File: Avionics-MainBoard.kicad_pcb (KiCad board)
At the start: 2 copper layers, 90.2 x 95.9 mm, 251 parts, among them J1 USB_C_Receptacle_USB2.0, J10 1824543, J11 1824527, J12 1824527, J13 1824527, J14 200528-0100, J15 200528-0100, J16 200528-0100, J17 1824543, J18 200528-0100, J19 200528-0100, J2 200528-0100, J3 Conn_01x06, J4 200528-0100, J5 Micro_SD_Card_Det2, J7 U.FL-R-SMT-1, J9 200528-0100, Q1 IRLML2803, Q14 MMBT2907, Q15 MMBT2907, Q16 NX3008NBKS, Q2 NX3008NBKS, Q21 MBT2222ADW1T1, Q22 NX3008NBKS, Q23 MBT2222ADW1T1, Q24 NX3008NBKS, Q25 MBT2222ADW1T1, Q26 NX3008NBKS, Q27 MBT2222ADW1T1, Q28 NX3008NBKS, Q29 MBT2222ADW1T1, Q3 MBT2222ADW1T1, Q30 MBT2222ADW1T1, Q4 NX3008NBKS, Q43 MBT2222ADW1T1, Q44 NX3008NBKS, Q45 MBT2222ADW1T1, Q46 NX3008NBKS, Q47 MBT2222ADW1T1, Q48 NX3008NBKS, Q49 MBT2222ADW1T1, Q5 MBT2222ADW1T1, Q50 NX3008NBKS, Q51 MBT2222ADW1T1, Q52 NX3008NBKS, Q53 MBT2222ADW1T1, SW1 SW_Omron_B3FS, SW2 SW_Omron_B3FS, U1 W25Q64JVSS, U10 BTS5090-1EJA, U14 ADM1176-1ARMZ-R7, U15 TPS7A4501DCQT, U16 ADM1176-1ARMZ-R7, U17 TPS54226PWPR, U18 ADM1176-1ARMZ-R7, U2 RP2040, U3 MAX706RESA+, U4 DS3231M, U5 BNO085, U6 USBLC6-2SC6, U7 E22-900M30S, U8 S1216V8, U9 BQ25883RGER, Y1 12MHz, Y2 32.768kHz

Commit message: temp
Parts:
- removed Q21, Q23, Q25, Q27, Q43, Q45, Q47, Q49, Q51, Q53: MBT2222ADW1T1, Package_TO_SOT_SMD:SOT-363_SC-70-6
- removed R99: DNI (0R), Resistor_SMD:R_0603_1608Metric
- added ?: , , F.Cu at (113.8, 57.1)
- added ?: , , F.Cu at (190.0, 142.9)
- added ?: , , F.Cu at (187.5, 57.1)
- added ?: , , F.Cu at (110.0, 142.9)
- added Q10: MBT2222ADW1T1, Package_TO_SOT_SMD:SOT-363_SC-70-6, F.Cu at (-51.2, -65.3)
- added Q11: MBT2222ADW1T1, Package_TO_SOT_SMD:SOT-363_SC-70-6, F.Cu at (-30.7, -69.3)
- added Q12: MBT2222ADW1T1, Package_TO_SOT_SMD:SOT-363_SC-70-6, F.Cu at (37.8, -60.9)
- added Q13: MBT2222ADW1T1, Package_TO_SOT_SMD:SOT-363_SC-70-6, F.Cu at (37.8, -41.3)
- added Q17: MBT2222ADW1T1, Package_TO_SOT_SMD:SOT-363_SC-70-6, F.Cu at (-51.2, -30.1)
- added Q6: MBT2222ADW1T1, Package_TO_SOT_SMD:SOT-363_SC-70-6, F.Cu at (48.1, -60.9)
- added Q7: MBT2222ADW1T1, Package_TO_SOT_SMD:SOT-363_SC-70-6, F.Cu at (-40.9, -69.3)
- added Q8: MBT2222ADW1T1, Package_TO_SOT_SMD:SOT-363_SC-70-6, F.Cu at (48.1, -41.3)
- added Q9: MBT2222ADW1T1, Package_TO_SOT_SMD:SOT-363_SC-70-6, F.Cu at (-40.9, -30.1)
- added Q99: NX3008NBKS, Package_TO_SOT_SMD:SOT-363_SC-70-6, F.Cu at (-40.9, -26.2)
- added R22: 200K, Resistor_SMD:R_0603_1608Metric, F.Cu at (-45.1, -15.8)
- BT1, C60, C61, C62, J12, J13, R116, U4, U7: moved to F.Cu
- Q14, R49, R50, R51, R52: moved to B.Cu
- Q2: value NX3008NBKS -> MBT2222ADW1T1
- R15: value 10K -> DNI (0R)
- R17: value 200K -> 10K
- moved J19 267.0 mm to (170.0, 143.1), turned to 0 degrees
- moved C20 260.1 mm to (-34.8, -45.4), turned to 0 degrees
- moved R8 259.1 mm to (-34.8, -37.9), turned to 0 degrees
- moved R9 258.5 mm to (-34.8, -35.4), turned to 0 degrees
- moved U5 256.4 mm to (-29.2, -48.8)
- moved C21 255.7 mm to (-34.8, -42.9), turned to 0 degrees
- moved Y2 250.4 mm to (-30.3, -44.3)
- moved C22 249.3 mm to (-34.8, -40.4), turned to 0 degrees
- moved C61 245.8 mm to (11.0, -59.1), turned to 0 degrees
- moved C18 244.3 mm to (-34.8, -50.5)
- moved C19 244.3 mm to (-34.8, -47.9)
- moved C60 242.3 mm to (11.0, -61.6), turned to 0 degrees
- moved R122 240.0 mm to (25.4, -60.5), turned to 0 degrees
- moved C63 236.4 mm to (11.0, -54.1), turned to 0 degrees
- moved J18 235.9 mm to (130.0, 143.1), turned to 0 degrees
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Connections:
- C23 pad 1: (no net) -> Net-(Q99B-G1)
- J15 pad 6: GND -> /MCU_IO/Jetson_CSn
- J15 pad 7: /MCU_IO/MCU_TX_Jetson -> /MCU_IO/SPI1_MOSI
- J15 pad 8: GND -> /MCU_IO/SPI1_CLK
- J15 pad 9: /MCU_IO/MCU_RX_Jetson -> /MCU_IO/SPI1_MISO
- J18 pad 10: /MCU_IO/I2C0_SCL -> /MCU_IO/I2C0_SDA
- J18 pad 9: /MCU_IO/I2C0_SDA -> /MCU_IO/I2C0_SCL
- J19 pad 5: /MCU_IO/I2C0_SCL -> /MCU_IO/I2C0_SDA
- J19 pad 6: /MCU_IO/I2C0_SDA -> /MCU_IO/I2C0_SCL
- J2 pad 10: /MCU_IO/I2C0_SCL -> /MCU_IO/I2C0_SDA
- J2 pad 9: /MCU_IO/I2C0_SDA -> /MCU_IO/I2C0_SCL
- J4 pad 10: /MCU_IO/I2C0_SCL -> /MCU_IO/I2C0_SDA
- J4 pad 9: /MCU_IO/I2C0_SDA -> /MCU_IO/I2C0_SCL
- Q14 pad 3: /MCU_IO/SD_MISO -> /LoRa Power/MISO
- Q2 pad 1: GND -> /MCU_IO/I2C1_SDA
- Q2 pad 2: (no net) -> Net-(Q2A-B1)
- Q2 pad 3: (no net) -> /MCU_IO/I2C1_SDA
- Q2 pad 4: GND -> /USB/CHG_SDA
- Q2 pad 5: (no net) -> Net-(Q28A-D1)
- Q2 pad 6: (no net) -> /USB/CHG_SDA
- Q3 pad 2: (no net) -> Net-(Q3A-B1)
- Q3 pad 4: /IMU/IMU_SCL -> /IMU/IMU_SDA
- Q3 pad 5: (no net) -> Net-(Q3B-B2)
- Q3 pad 6: /IMU/IMU_SCL -> /IMU/IMU_SDA
- Q4 pad 6: Net-(Q4A-D1) -> Net-(Q10B-B2)
- Q44 pad 6: Net-(Q44A-D1) -> Net-(Q3B-B2)
- Q5 pad 1: /MCU_IO/I2C1_SCL -> /MCU_IO/I2C0_SCL
- Q5 pad 3: /MCU_IO/I2C1_SCL -> /MCU_IO/I2C0_SCL
- Q5 pad 4: /LoRa Power/I2C Protection3/SCL_DEVICE -> /RTC/RTC_SCL
- Q5 pad 5: Net-(Q4A-D1) -> Net-(Q46A-D1)
- Q5 pad 6: /LoRa Power/I2C Protection3/SCL_DEVICE -> /RTC/RTC_SCL
- R104 pad 2: /MCU_IO/I2C0_SCL -> /MCU_IO/I2C0_SDA
- R105 pad 1: Net-(Q43A-B1) -> Net-(Q2A-B1)
- R13 pad 1: (no net) -> Net-(Q9A-B1)
- R13 pad 2: (no net) -> Net-(Q99A-D1)
- R14 pad 2: (no net) -> Net-(Q99A-G2)
- R15 pad 1: +3V3 -> /IMU/IMU_SCL
- R15 pad 2: (no net) -> /MCU_IO/I2C0_SDA
- R16 pad 2: /IMU/IMU_SCL -> Net-(Q99A-D1)
- R163 pad 1: Net-(Q45A-B1) -> Net-(Q3A-B1)
- R163 pad 2: Net-(Q44A-D1) -> Net-(Q3B-B2)
- R165 pad 2: /MCU_IO/I2C0_SDA -> /MCU_IO/I2C0_SCL
- R166 pad 2: Net-(Q44A-D1) -> Net-(Q3B-B2)
- R169 pad 1: Net-(Q47A-B1) -> Net-(Q5A-B1)
- R17 pad 1: /IMU/IMU_SCL -> +3V3
- R17 pad 2: (no net) -> /IMU/IMU_SCL
- R171 pad 2: /MCU_IO/I2C0_SDA -> /MCU_IO/I2C0_SCL
- R18 pad 1: Net-(Q5A-B1) -> Net-(Q10A-B1)
- R18 pad 2: Net-(Q4A-D1) -> Net-(Q10B-B2)
- R20 pad 2: Net-(Q4A-D1) -> Net-(Q10B-B2)
- R51 pad 2: /MCU_IO/SD_CLK -> /LoRa Power/CLK
- R52 pad 2: /MCU_IO/SD_MOSI -> /LoRa Power/MOSI
- R57 pad 2: /LoRa Power/CSn -> /LoRa Power/LoRa_CSn
- U2 pad 11: /LoRa Power/MISO -> unconnected-(U2-GPIO8-Pad11)
- U2 pad 12: /LoRa Power/CSn -> unconnected-(U2-GPIO9-Pad12)
- U2 pad 13: /LoRa Power/CLK -> unconnected-(U2-GPIO10-Pad13)
- U2 pad 14: /LoRa Power/MOSI -> unconnected-(U2-GPIO11-Pad14)
- U2 pad 15: /MCU_IO/LoRa_EN -> unconnected-(U2-GPIO12-Pad15)
- U2 pad 16: /LoRa Power/LoRa_RSTn -> unconnected-(U2-GPIO13-Pad16)
- U2 pad 17: /LoRa Power/LoRa_BUSY -> unconnected-(U2-GPIO14-Pad17)
- U2 pad 18: /MCU_IO/WDT_WDI -> unconnected-(U2-GPIO15-Pad18)
- U2 pad 2: /MCU_IO/I2C0_SDA -> unconnected-(U2-GPIO0-Pad2)
- U2 pad 27: /MCU_IO/MCU_TX_Jetson -> /LoRa Power/MISO
- U2 pad 28: /MCU_IO/MCU_RX_Jetson -> /LoRa Power/LoRa_CSn
- U2 pad 29: /IMU/IMU_INTn -> /LoRa Power/CLK
- U2 pad 3: /MCU_IO/I2C0_SCL -> unconnected-(U2-GPIO1-Pad3)
- U2 pad 30: /IMU/IMU_RSTn -> /LoRa Power/MOSI
- U2 pad 31: /MCU_IO/SD_MISO -> /LoRa Power/LoRa_RX_EN
- U2 pad 32: /MCU_IO/SD_CSn -> /LoRa Power/LoRa_RSTn
- U2 pad 34: /MCU_IO/SD_CLK -> /LoRa Power/LoRa_TX_EN
- U2 pad 35: /MCU_IO/SD_MOSI -> /LoRa Power/LoRa_BUSY
- U2 pad 36: /MCU_IO/Jetson_EN -> /LoRa Power/LoRa_DIO2
- U2 pad 37: /MCU_IO/Battery_ALERT -> /LoRa Power/LoRa_DIO1
- U2 pad 38: /LoRa Power/LoRa_DIO1 -> /MCU_IO/SD_CSn
- U2 pad 39: /LoRa Power/LoRa_DIO2 -> unconnected-(U2-GPIO27_ADC1-Pad39)
- U2 pad 4: /MCU_IO/I2C1_SDA -> unconnected-(U2-GPIO2-Pad4)
- U2 pad 40: /LoRa Power/LoRa_RX_EN -> unconnected-(U2-GPIO28_ADC2-Pad40)
- U2 pad 41: /LoRa Power/LoRa_TX_EN -> unconnected-(U2-GPIO29_ADC3-Pad41)
- U2 pad 5: /MCU_IO/I2C1_SCL -> unconnected-(U2-GPIO3-Pad5)
- U2 pad 6: /GPS Power/GPS_RX_MCU -> unconnected-(U2-GPIO4-Pad6)
- U2 pad 7: /GPS Power/GPS_TX_MCU -> unconnected-(U2-GPIO5-Pad7)
- U2 pad 8: /MCU_IO/GPS_EN -> unconnected-(U2-GPIO6-Pad8)
- U2 pad 9: /MCU_IO/3V3_RST -> unconnected-(U2-GPIO7-Pad9)
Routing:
- net /LoRa Power/LoRa_DIO2: track 0.00 -> 60.3 mm
- net /LoRa Power/LoRa_TX_EN: track 0.00 -> 58.3 mm
- net /LoRa Power/LoRa_RX_EN: track 0.00 -> 56.9 mm
- net /LoRa Power/MOSI: track 0.00 -> 43.8 mm, vias 0 -> 1
- net /LoRa Power/CLK: track 0.00 -> 41.8 mm, vias 0 -> 1
- net /LoRa Power/LoRa_DIO1: track 0.00 -> 36.2 mm
- net /LoRa Power/MISO: track 0.00 -> 35.0 mm, vias 0 -> 2
- net /LoRa Power/LoRa_BUSY: track 0.00 -> 33.9 mm
- net /LoRa Power/LoRa_RSTn: track 0.00 -> 31.8 mm
- net /LoRa Power/LoRa_CSn: track 0.00 -> 25.1 mm
- net /MCU_IO/SD_CSn: track 0.00 -> 24.3 mm
- net /Main Power/+3V3_PS: track 20.1 -> 0.00 mm
- net Net-(Q15-B): track 0.00 -> 7.83 mm
- net /LoRa Power/LoRa_MISO: track 0.00 -> 7.75 mm
- net /LoRa Power/LoRa_MOSI: track 0.00 -> 7.69 mm
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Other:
- copper layers 2 -> 4

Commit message: v1 done
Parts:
- removed ? (x4): , 
- removed C10: 2u2, Capacitor_SMD:C_0603_1608Metric
- removed D4, D5: 10V, Diode_SMD:D_SOD-123F
- removed R53, R54: 10K, Resistor_SMD:R_0603_1608Metric
- added C25: 2u2, Capacitor_SMD:C_0603_1608Metric, F.Cu at (149.5, 96.0)
- added D1: NUP2105L, Package_TO_SOT_SMD:SOT-23, F.Cu at (183.0, 128.0)
- added D2: NUP2105L, Package_TO_SOT_SMD:SOT-23, F.Cu at (183.0, 131.6)
- added H1: MountingHole_Pad, MountingHole:MountingHole_3.2mm_M3_DIN965_Pad_TopBottom, F.Cu at (113.8, 57.1)
- added H2: MountingHole_Pad, MountingHole:MountingHole_3.2mm_M3_DIN965_Pad_TopBottom, F.Cu at (187.4, 57.1)
- added H3: MountingHole_Pad, MountingHole:MountingHole_3.2mm_M3_DIN965_Pad_TopBottom, F.Cu at (190.1, 142.8)
- added H4: MountingHole_Pad, MountingHole:MountingHole_3.2mm_M3_DIN965_Pad_TopBottom, F.Cu at (110.0, 142.9)
- added J6: 200528-0100, Argus-Connectors:Molex_200528-0100_1x10-1MP_P1.00mm_Horizontal, F.Cu at (190.1, 130.0)
- added R23: 10K, Resistor_SMD:R_0603_1608Metric, B.Cu at (147.0, 113.0)
- added R24: 10K, Resistor_SMD:R_0603_1608Metric, B.Cu at (147.0, 116.5)
- added R25: 10k, Resistor_SMD:R_0603_1608Metric, F.Cu at (150.5, 113.0)
- added R26: 10k, Resistor_SMD:R_0603_1608Metric, F.Cu at (152.0, 113.0)
- added R27: 680R, Resistor_SMD:R_0603_1608Metric, F.Cu at (157.5, 125.5)
- added R28: 120R, Resistor_SMD:R_0603_1608Metric, F.Cu at (151.5, 125.0)
- added R29: 680R, Resistor_SMD:R_0603_1608Metric, F.Cu at (157.5, 128.5)
- added R30: 680R, Resistor_SMD:R_0603_1608Metric, F.Cu at (162.0, 132.0)
- added R31: 120R, Resistor_SMD:R_0603_1608Metric, F.Cu at (148.5, 125.0)
- added R32: 680R, Resistor_SMD:R_0603_1608Metric, F.Cu at (162.0, 129.0)
- added R33: 2k2, Resistor_SMD:R_0603_1608Metric, F.Cu at (121.3, 67.0)
- added U12: ADM1491EBR, Package_SO:SOIC-14_3.9x8.7mm_P1.27mm, F.Cu at (150.7, 120.0)
- BT1, C24, C30, C32, C33, C34, C36, C37, C38, C39, C4, C40, C41, C42, C43, C48, C50, C53, C55, C56, C57, J7, L1, Q1, Q10, Q11, Q15, Q16, Q17, Q2, Q26, Q28, Q4, Q46, Q5, Q50, Q7, R10, R100, R101, R104, R105, R106, R107, R108, R11, R110, R111, R112, R113, R12, R161, R162, R169, R170, R171, R172, R173, R174, R18, R181, R182, R183, R184, R185, R186, R19, R20, R21, R3, R4, R55, R56, R57, R58, R59, R6, R60, R61, R62, R63, R67, R69, R7, R70, R83, R94, R95, R96, R97, R98, U1, U15, U16, U3, U4, U7, U8, U9: moved to B.Cu
- C58, C59: value 100u -> 10u
- J1: footprint Connector_USB:USB_C_Receptacle_HRO_TYPE-C-31-M-12 -> Connector_USB:USB_C_Receptacle_GCT_USB4105-xx-A_16P_TopMnt_Horizontal
- J14, J15, J16, J18, J19, J2, J4, J9: footprint Connector_FFC-FPC:Molex_200528-0100_1x10-1MP_P1.00mm_Horizontal -> Argus-Connectors:Molex_200528-0100_1x10-1MP_P1.00mm_Horizontal
- J5, Q14, R49, R50, R51, R52: moved to F.Cu
- R46, R47: value 5.1K -> 5k1
- R65: value 5.23K -> 5k23; moved to B.Cu
- R66: value 30.1K -> 30k1; moved to B.Cu
- SW1, SW2: footprint Button_Switch_SMD:SW_SPST_Omron_B3FS-100xP -> Button_Switch_SMD:SW_SPST_Omron_B3FS-105xP
- moved C55 277.9 mm to (127.5, 120.0), turned to 90 degrees
- moved C56 272.4 mm to (127.5, 116.5), turned to 90 degrees
- moved C57 269.0 mm to (118.0, 119.5)
- moved R110 260.2 mm to (127.5, 113.0), turned to 90 degrees
- moved R111 259.3 mm to (133.5, 111.5)
- moved U15 254.9 mm to (133.5, 116.0)
- moved R105 253.6 mm to (166.5, 75.0), turned to -90 degrees
- moved R113 252.5 mm to (118.0, 114.0), turned to 180 degrees
- moved R108 251.8 mm to (168.5, 75.0), turned to -90 degrees
- moved R107 251.6 mm to (168.5, 72.0), turned to 180 degrees
- moved Q2 248.7 mm to (164.0, 75.0), turned to -90 degrees
- moved R106 247.0 mm to (162.0, 72.0)
- moved C48 246.8 mm to (159.0, 72.0)
- moved R161 246.7 mm to (165.5, 72.0)
- moved C2 245.9 mm to (145.5, 98.5), turned to 90 degrees
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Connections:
- net Net-(J1-D+-PadA6) renamed /USB/D_UP+
- net Net-(J1-D--PadA7) renamed /USB/D_UP-
- J15 pad 4: /MCU_IO/Jetson_EN -> unconnected-(J15-Pin_4-Pad4)
- J15 pad 6: /MCU_IO/Jetson_CSn -> /MCU_IO/SPI1_MISO
- J15 pad 7: /MCU_IO/SPI1_MOSI -> /MCU_IO/Jetson_CSn
- J15 pad 9: /MCU_IO/SPI1_MISO -> /MCU_IO/SPI1_MOSI
- J19 pad 7: /MCU_IO/Battery_ALERT -> unconnected-(J19-Pin_7-Pad7)
- U2 pad 11: unconnected-(U2-GPIO8-Pad11) -> /MCU_IO/SPI1_MISO
- U2 pad 12: unconnected-(U2-GPIO9-Pad12) -> /MCU_IO/Jetson_CSn
- U2 pad 13: unconnected-(U2-GPIO10-Pad13) -> /MCU_IO/SPI1_CLK
- U2 pad 14: unconnected-(U2-GPIO11-Pad14) -> /MCU_IO/SPI1_MOSI
- U2 pad 15: unconnected-(U2-GPIO12-Pad15) -> /GPS Power/GPS_RX_MCU
- U2 pad 16: unconnected-(U2-GPIO13-Pad16) -> /GPS Power/GPS_TX_MCU
- U2 pad 17: unconnected-(U2-GPIO14-Pad17) -> /MCU_IO/RS485_TX_EN
- U2 pad 18: unconnected-(U2-GPIO15-Pad18) -> /MCU_IO/RS485_RX_EN
- U2 pad 2: unconnected-(U2-GPIO0-Pad2) -> /MCU_IO/I2C0_SDA
- U2 pad 3: unconnected-(U2-GPIO1-Pad3) -> /MCU_IO/I2C0_SCL
- U2 pad 39: unconnected-(U2-GPIO27_ADC1-Pad39) -> /MCU_IO/GPS_EN
- U2 pad 4: unconnected-(U2-GPIO2-Pad4) -> /MCU_IO/I2C1_SDA
- U2 pad 40: unconnected-(U2-GPIO28_ADC2-Pad40) -> /MCU_IO/LoRa_EN
- U2 pad 41: unconnected-(U2-GPIO29_ADC3-Pad41) -> /IMU/IMU_INTn
- U2 pad 5: unconnected-(U2-GPIO3-Pad5) -> /MCU_IO/I2C1_SCL
- U2 pad 6: unconnected-(U2-GPIO4-Pad6) -> /MCU_IO/UART1_TX
- U2 pad 7: unconnected-(U2-GPIO5-Pad7) -> /MCU_IO/UART1_RX
- U2 pad 8: unconnected-(U2-GPIO6-Pad8) -> /MCU_IO/WDT_WDI
- U2 pad 9: unconnected-(U2-GPIO7-Pad9) -> /MCU_IO/3V3_RST
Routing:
- net GND: track 0.00 -> 328.0 mm, vias 0 -> 123
- net /MCU_IO/I2C0_SDA: track 0.00 -> 287.9 mm, vias 0 -> 8
- net /MCU_IO/I2C0_SCL: track 0.00 -> 282.9 mm, vias 0 -> 8
- net VSYS: track 0.00 -> 282.5 mm, vias 0 -> 16
- net /MCU_IO/I2C1_SCL: track 0.00 -> 225.6 mm, vias 0 -> 6
- net /MCU_IO/I2C1_SDA: track 0.00 -> 220.5 mm, vias 0 -> 7
- net +3V3: track 0.00 -> 171.7 mm, vias 0 -> 65
- net /MCU_IO/GPS_EN: track 0.00 -> 66.7 mm, vias 0 -> 2
- net GNDREF: track 0.00 -> 60.6 mm, vias 0 -> 17
- net /MCU_IO/RS485_TX_EN: track 0.00 -> 56.5 mm, vias 0 -> 2
- net /USB/VUSB: track 0.00 -> 54.6 mm, vias 0 -> 4
- net /MCU_IO/3V3_RST: track 0.00 -> 52.9 mm, vias 0 -> 2
- net /MCU_IO/LoRa_EN: track 0.00 -> 52.7 mm, vias 0 -> 1
- net /MCU_IO/SD_CSn: track 24.3 -> 76.9 mm
- net /MCU_IO/RS485_RX_EN: track 0.00 -> 52.4 mm, vias 0 -> 2
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- added copper zone on F.Cu, net +3V3
- added copper zone on In1.Cu, net +3V3
- added copper zone on F.Cu, net /Main Power/+3V3_PS
- added copper zone on B.Cu, net /USB/BATT
- added copper zone on B.Cu, net /USB/SYS
- added copper zone on B.Cu, net GND
- added copper zone on F.Cu, net GND
- added copper zone on In2.Cu, net GND
- added copper zone on F.Cu, net GNDREF
- added copper zone on In2.Cu, net GNDREF
- added copper zone on B.Cu, net GPS_VDD
- added copper zone on In1.Cu, net GPS_VDD
- added copper zone on B.Cu, net LoRa_VDD
- added copper zone on In1.Cu, net LoRa_VDD
- added copper zone on F.Cu, net Net-(J12-Pad1)
- added copper zone on F.Cu, net Net-(U14-VCC)
- added copper zone on B.Cu, net Net-(U15-OUT)
- added copper zone on F.Cu, net Net-(U17-SW1)
- added copper zone on B.Cu, net Net-(U9-PMID_1)
- added copper zone on B.Cu, net Net-(U9-SW_1)
- added copper zone on B.Cu, net VBATT
- added copper zone on F.Cu, net VBATT
- added copper zone on F.Cu, net VSYS

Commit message: Updated i2c device addresses and mcu caps
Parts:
- removed the C14 at (142.5, 79.8)
- added C10: 100n, Capacitor_SMD:C_0603_1608Metric, F.Cu at (156.5, 120.0)
- added C3: 100n, Capacitor_SMD:C_0603_1608Metric, B.Cu at (152.2, 77.0)
- C12: value 100n -> 1u
- C14: renamed from C5; value 100n -> 2u2
- C25, C8: value 2u2 -> 100n
- C6: value 2u2 -> 1u
- C7: renamed from C9; value 100n -> 1u
- moved C12 6.97 mm to (142.5, 79.8)
- moved C14 1.50 mm to (150.8, 81.5)
- moved C7 1.50 mm to (149.2, 81.5)
- moved R114 0.35 mm to (166.5, 77.8)
- moved R115 0.10 mm to (164.8, 77.8)
- renumbered C16 to C11, C15 to C13, C7 to C15, C11 to C16, C3 to C5, C13 to C9
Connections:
- U14 pad 8: unconnected-(U14-A0-Pad8) -> GND
- U14 pad 9: unconnected-(U14-A1-Pad9) -> GND
- U16 pad 9: unconnected-(U16-A1-Pad9) -> GND
- U18 pad 8: unconnected-(U18-A0-Pad8) -> GND
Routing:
- net LoRa_VDD: track 10.0 -> 46.8 mm
- net GPS_VDD: track 11.0 -> 40.5 mm
- net GND: track 328.0 -> 338.8 mm, vias 123 -> 125
- net +3V3: track 171.7 -> 180.1 mm
- removed copper zone on In1.Cu, net GPS_VDD
- removed copper zone on In1.Cu, net LoRa_VDD

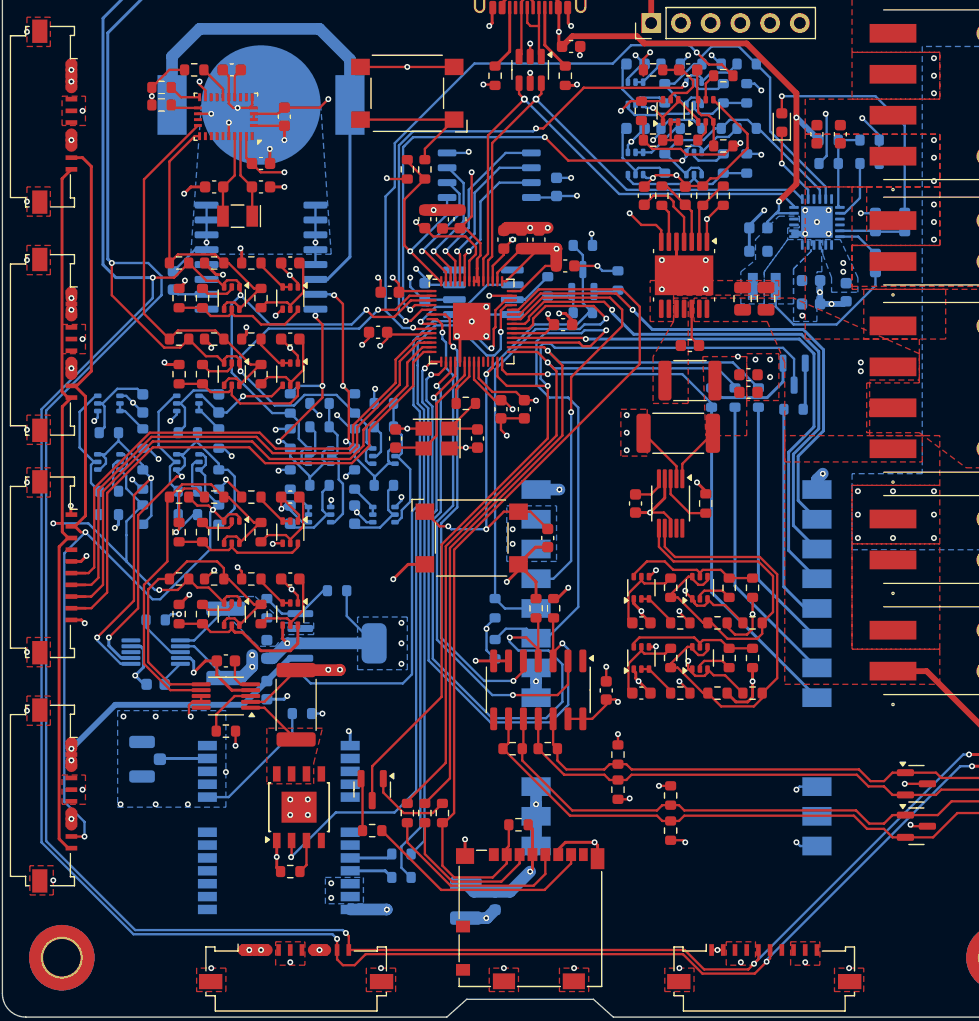
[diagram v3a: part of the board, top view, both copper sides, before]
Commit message: Added extra connector
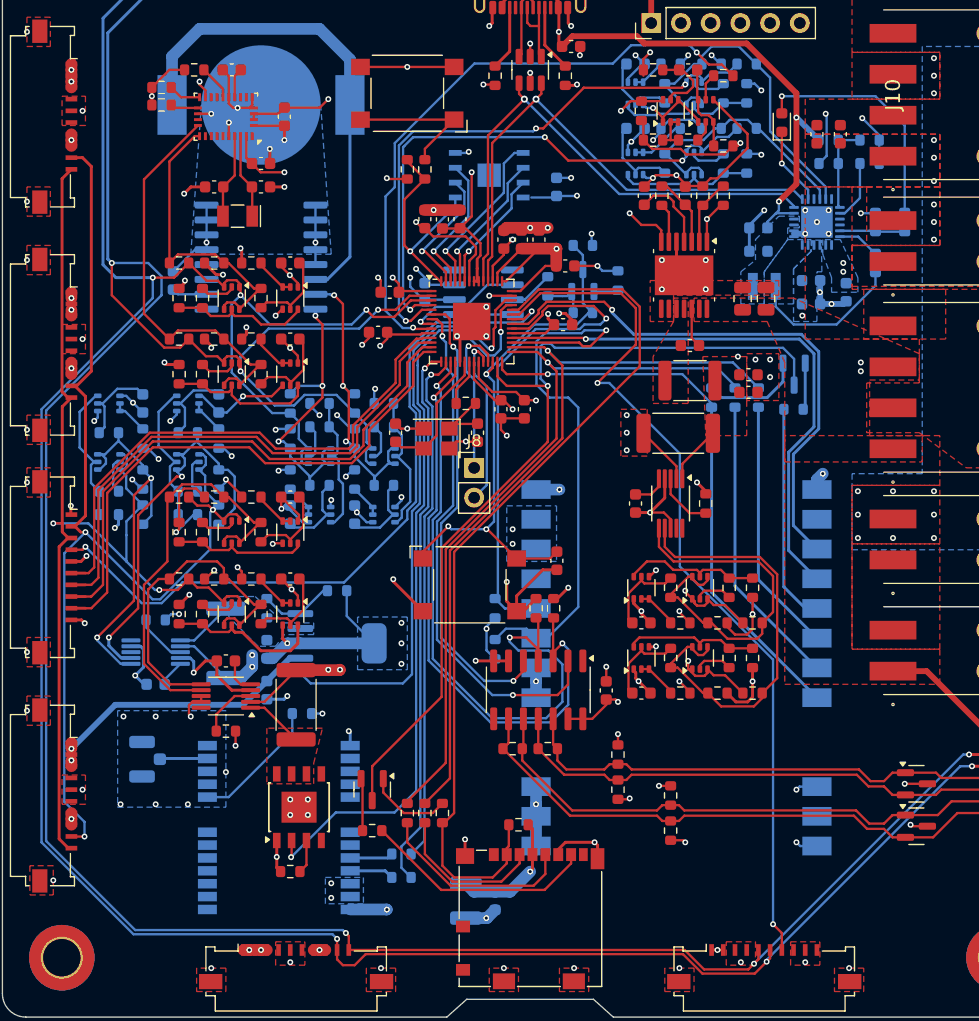
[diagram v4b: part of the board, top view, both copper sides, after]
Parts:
- added J8: Conn_01x02, Connector_PinHeader_2.54mm:PinHeader_1x02_P2.54mm_Vertical, F.Cu at (145.2, 101.0)
- U1: value W25Q64JVSS -> MR25H40MDF; footprint Package_SO:SOIC-8_5.23x5.23mm_P1.27mm -> Package_DFN_QFN:DFN-8-1EP_6x5mm_P1.27mm_EP2x2mm
- moved SW2 4.00 mm to (144.8, 111.0)
- moved C17 2.09 mm to (152.3, 108.9)
- moved C1 0.50 mm to (138.5, 98.0)
- moved C2 0.50 mm to (145.5, 98.0)
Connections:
- J15 pad 4: unconnected-(J15-Pin_4-Pad4) -> /MCU_IO/Jetson_EN
- J19 pad 7: unconnected-(J19-Pin_7-Pad7) -> /MCU_IO/Battery_ALERT
- U2 pad 24: unconnected-(U2-SWCLK-Pad24) -> Net-(J8-Pin_2)
- U2 pad 25: unconnected-(U2-SWD-Pad25) -> Net-(J8-Pin_1)
- U2 pad 36: /LoRa Power/LoRa_DIO2 -> /MCU_IO/Jetson_EN
- U2 pad 37: /LoRa Power/LoRa_DIO1 -> /MCU_IO/Battery_ALERT
- U7 pad 13: /LoRa Power/LoRa_DIO1 -> unconnected-(U7-DIO1-Pad13)
- U7 pad 8: /LoRa Power/LoRa_DIO2 -> unconnected-(U7-DIO2-Pad8)
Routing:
- net /MCU_IO/Battery_ALERT: track 0.00 -> 75.2 mm, vias 0 -> 2
- net /MCU_IO/Jetson_EN: track 0.00 -> 62.7 mm, vias 0 -> 2
- net /LoRa Power/LoRa_DIO1: track 45.4 -> 0.00 mm, vias 1 -> 0
- net /LoRa Power/LoRa_DIO2: track 37.5 -> 0.00 mm, vias 1 -> 0
- net Net-(J8-Pin_2): track 0.00 -> 14.8 mm, vias 0 -> 1
- net Net-(J8-Pin_1): track 0.00 -> 13.4 mm, vias 0 -> 1
- net /MCU_IO/RUN: track 44.7 -> 47.2 mm
- net GND: track 338.8 -> 341.2 mm, vias 125 -> 124
- net /MCU_IO/QSPI_SD3: track 12.4 -> 10.5 mm
- net /MCU_IO/QSPI_CLK: track 14.0 -> 12.1 mm
- net /MCU_IO/QSPI_SD0: track 15.6 -> 14.5 mm
- net /MCU_IO/LoRa_EN: track 52.7 -> 51.8 mm
- net /MCU_IO/GPS_EN: track 66.7 -> 65.9 mm
